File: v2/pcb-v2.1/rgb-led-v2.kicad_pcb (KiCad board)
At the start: 2 copper layers, 90 x 50 mm, 12 parts, among them SW1 SPST

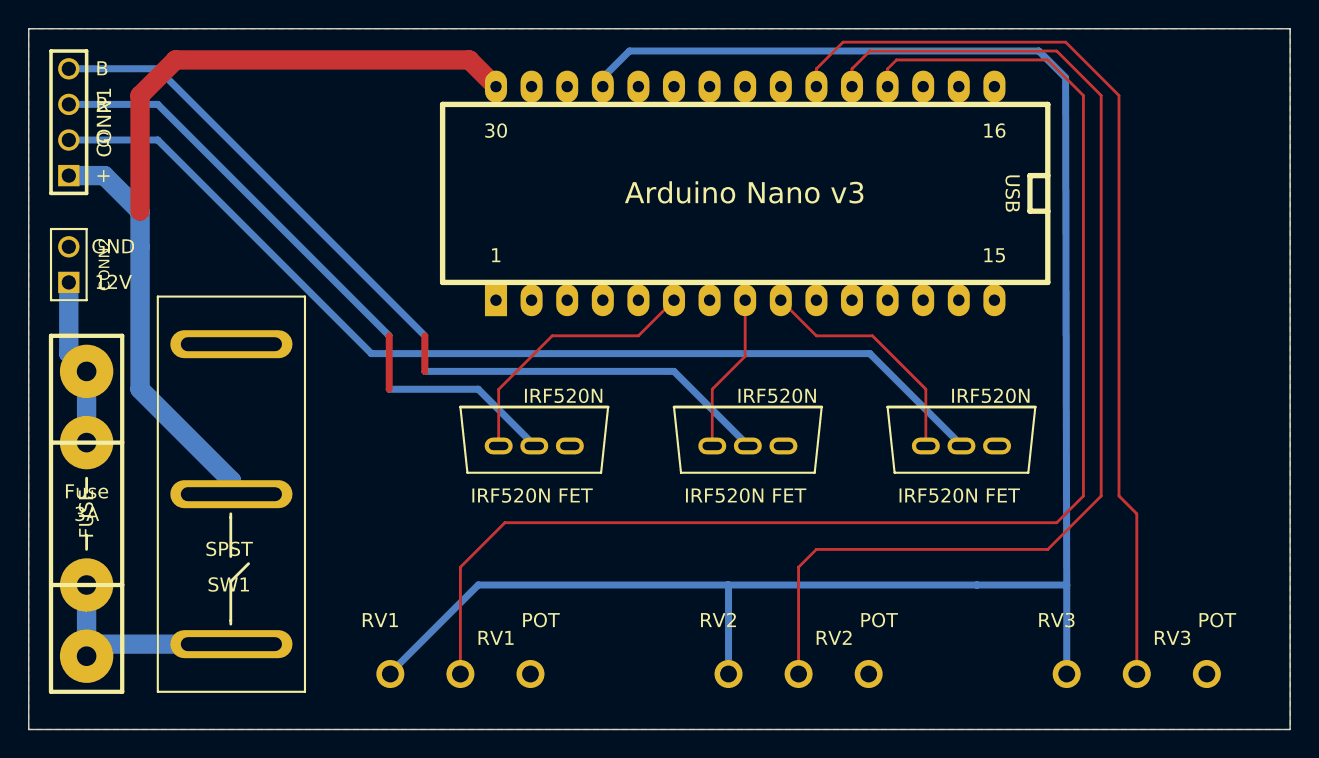
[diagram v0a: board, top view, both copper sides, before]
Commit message: PCB: Remove unnecessary vias
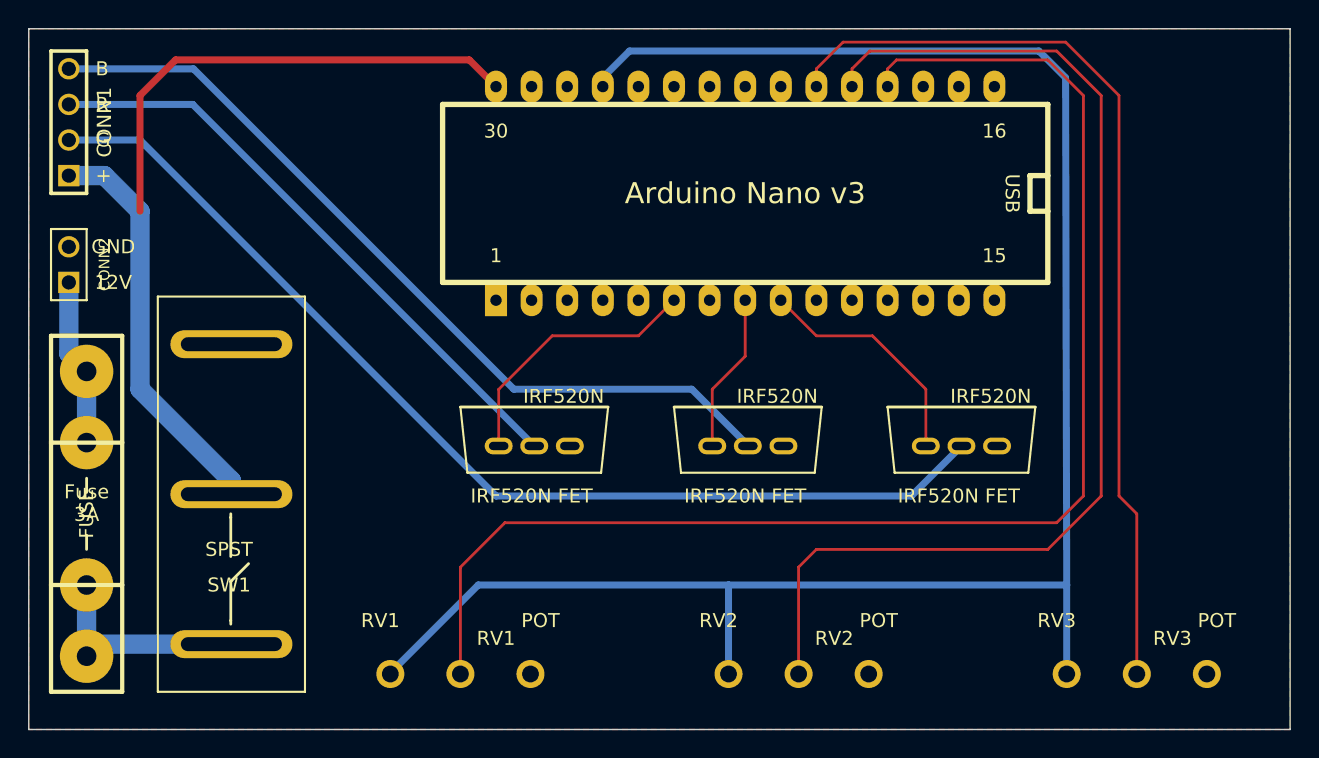
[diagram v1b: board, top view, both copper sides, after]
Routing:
- net N-0000012: track 72.8 -> 75.7 mm
- net N-0000013: track 45.6 -> 43.4 mm, vias 2 -> 0
- net N-0000014: track 61.1 -> 59.6 mm, vias 2 -> 0
